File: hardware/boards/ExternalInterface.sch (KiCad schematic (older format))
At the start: 1 part, among them U1 ECP5UM5G-381caBGA

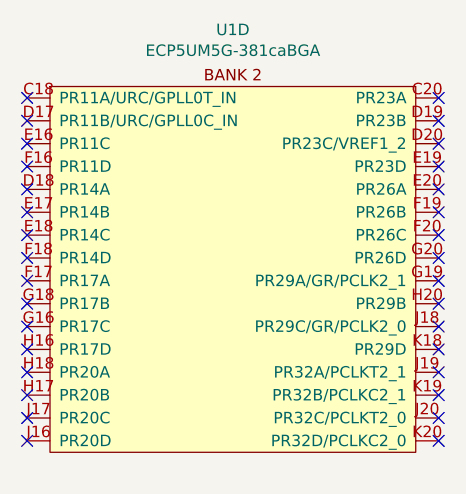
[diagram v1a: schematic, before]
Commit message: Moving banks around and rotated the FPGA to try and give the SERDES channels the best routing to the PCIe connector
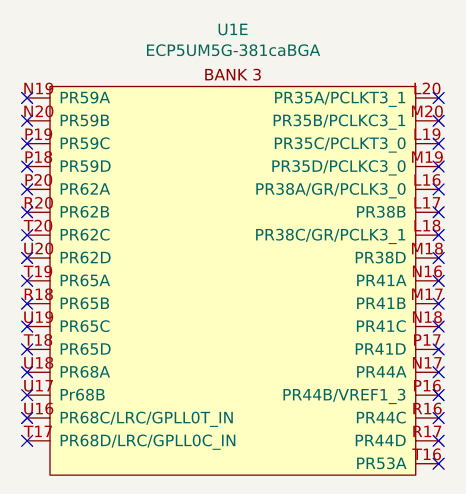
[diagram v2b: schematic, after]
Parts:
- removed U1: ECP5UM5G-381caBGA, lethalbit:318caBGA, symbol lethalbit:ECP5UM5G-381caBGA
- added U1: ECP5UM5G-381caBGA, lethalbit:318caBGA, symbol lethalbit:ECP5UM5G-381caBGA
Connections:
- no-connect marks 32 -> 33
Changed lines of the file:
@@
 Comment4 ""
 $EndDescr
-$Comp
-L lethalbit:ECP5UM5G-381caBGA U1
-U 4 1 5F2381FE
-P 5550 3250
-F 0 "U1" H 5550 3598 50  0000 C CNN
-F 1 "ECP5UM5G-381caBGA" H 5550 3507 50  0000 C CNN
-F 2 "lethalbit:318caBGA" H 4200 3400 50  0001 C CNN
-F 3 "" H 4200 3400 50  0001 C CNN
-F 4 "Lattice" H 5550 3250 50  0001 C CNN "MFR"
-F 5 "LFE5UM5G-85F-8BG381I" H 5550 3250 50  0001 C CNN "MPN"
-F 6 "220-2112-ND" H 5550 3250 50  0001 C CNN "DIGIKEY_PN"
-	4    5550 3250
-	1    0    0    -1
-$EndComp
 NoConn ~ 4650 3200
 NoConn ~ 4650 3300
@@
 NoConn ~ 6450 3300
 NoConn ~ 6450 3200
+$Comp
+L lethalbit:ECP5UM5G-381caBGA U?
+U 5 1 5F8BF516
+P 5550 3250
+AR Path="/5EF67D90/5F8BF516" Ref="U?"  Part="5"
+AR Path="/5F2CAFD2/5F8BF516" Ref="U?"  Part="5"
+AR Path="/5EF6A128/5F8BF516" Ref="U1"  Part="5"
+F 0 "U1" H 5550 3598 50  0000 C CNN
+F 1 "ECP5UM5G-381caBGA" H 5550 3507 50  0000 C CNN
+F 2 "lethalbit:318caBGA" H 4200 3400 50  0001 C CNN
+F 3 "" H 4200 3400 50  0001 C CNN
+F 4 "Lattice" H 5550 3250 50  0001 C CNN "MFR"
+F 5 "LFE5UM5G-85F-8BG381I" H 5550 3250 50  0001 C CNN "MPN"
+F 6 "220-2112-ND" H 5550 3250 50  0001 C CNN "DIGIKEY_PN"
+	5    5550 3250
+	-1   0    0    -1
+$EndComp
+NoConn ~ 6450 4800
 $EndSCHEMATC

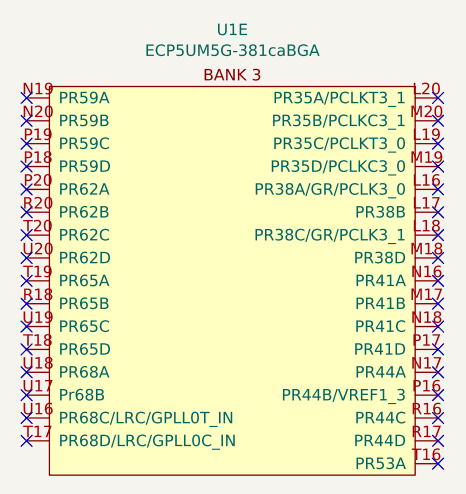
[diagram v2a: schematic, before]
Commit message: Moved some things around swapping the DDR from banks 7 and 8 to banks 2 and 3, and moved the GPIFF 2 stuff to bank 7 to stop them from crossing over
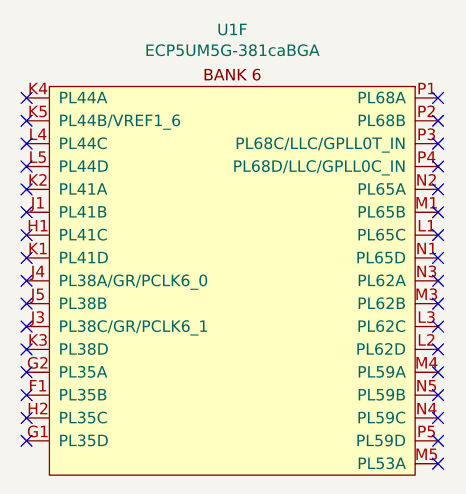
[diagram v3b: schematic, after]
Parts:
- removed U1: ECP5UM5G-381caBGA, lethalbit:318caBGA, symbol lethalbit:ECP5UM5G-381caBGA
- added U1: ECP5UM5G-381caBGA, lethalbit:318caBGA, symbol lethalbit:ECP5UM5G-381caBGA
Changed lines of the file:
@@
 NoConn ~ 6450 3300
 NoConn ~ 6450 3200
+NoConn ~ 6450 4800
 $Comp
 L lethalbit:ECP5UM5G-381caBGA U?
-U 5 1 5F8BF516
+U 6 1 5FCD2B63
 P 5550 3250
-AR Path="/5EF67D90/5F8BF516" Ref="U?"  Part="5"
-AR Path="/5F2CAFD2/5F8BF516" Ref="U?"  Part="5"
-AR Path="/5EF6A128/5F8BF516" Ref="U1"  Part="5"
+AR Path="/5EDF3898/5FCD2B63" Ref="U?"  Part="6"
+AR Path="/5FCD2B63" Ref="U?"  Part="6"
+AR Path="/5EF6A128/5FCD2B63" Ref="U1"  Part="6"
 F 0 "U1" H 5550 3598 50  0000 C CNN
 F 1 "ECP5UM5G-381caBGA" H 5550 3507 50  0000 C CNN
@@
 F 5 "LFE5UM5G-85F-8BG381I" H 5550 3250 50  0001 C CNN "MPN"
 F 6 "220-2112-ND" H 5550 3250 50  0001 C CNN "DIGIKEY_PN"
-	5    5550 3250
+	6    5550 3250
 	-1   0    0    -1
 $EndComp
-NoConn ~ 6450 4800
 $EndSCHEMATC

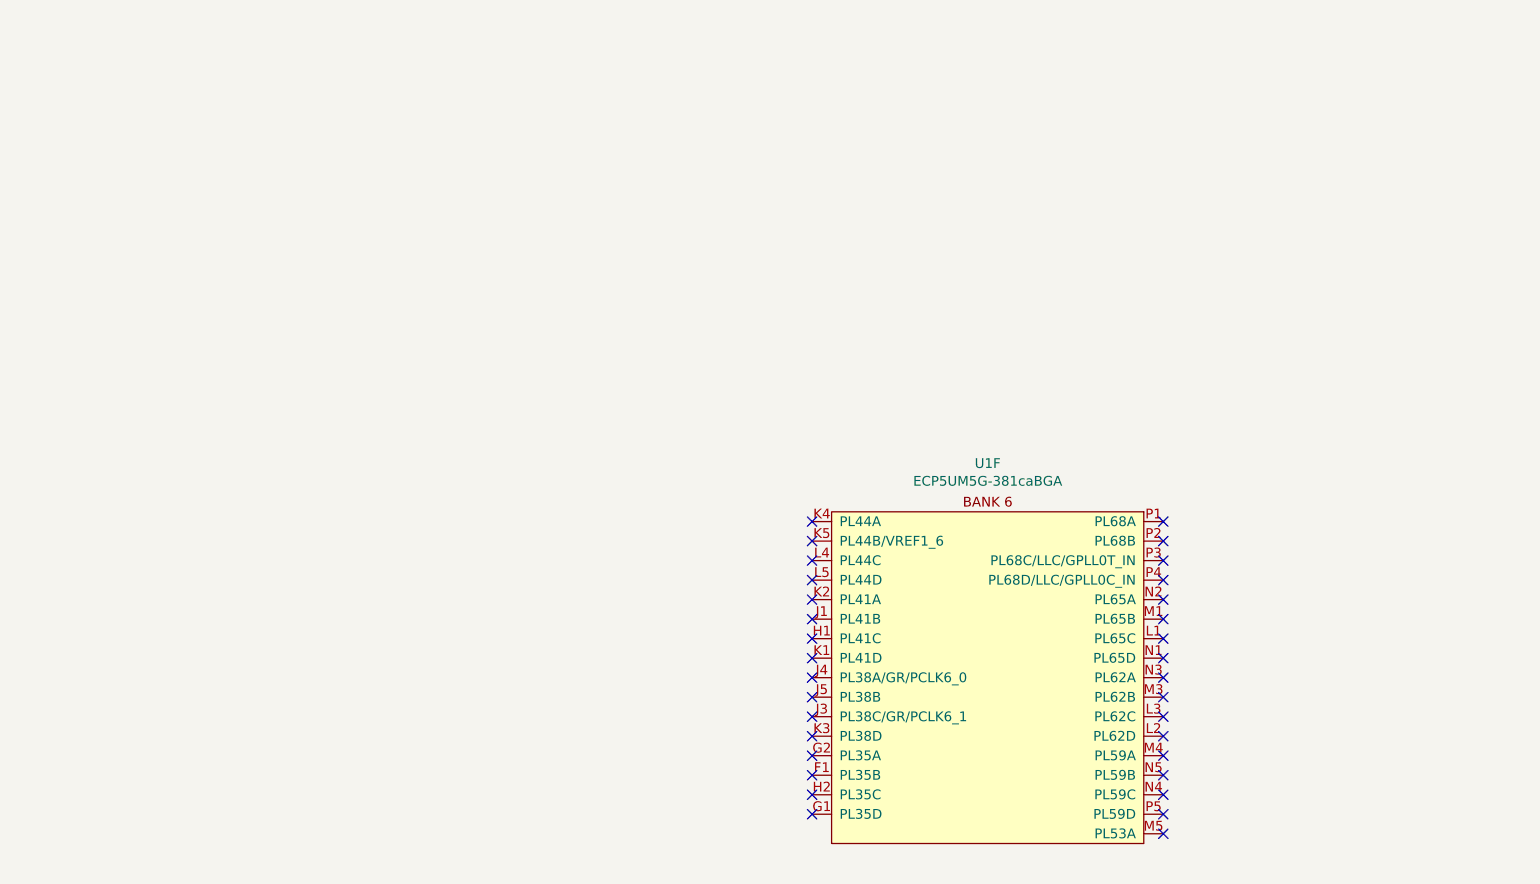
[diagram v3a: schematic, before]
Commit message: Moved some more banks around to try and keeps things from crossing over as much as possible
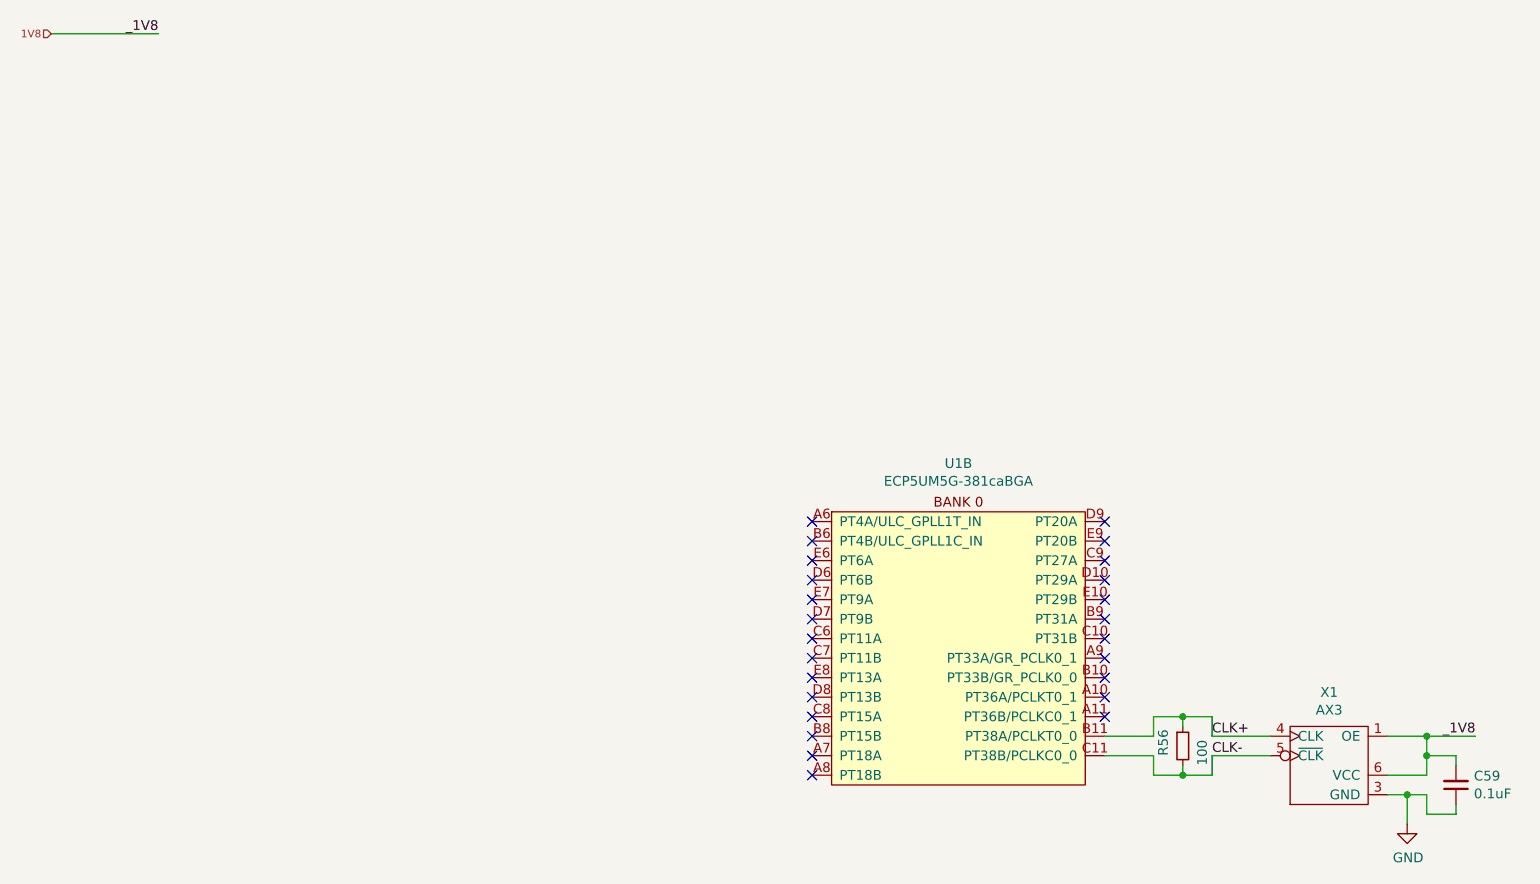
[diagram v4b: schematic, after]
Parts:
- removed U1: ECP5UM5G-381caBGA, lethalbit:318caBGA, symbol lethalbit:ECP5UM5G-381caBGA
- added C59: 0.1uF, Capacitor_SMD:C_0603_1608Metric, symbol Device:C_Small
- added R56: 100, Resistor_SMD:R_0402_1005Metric, symbol Device:R_Small
- added U1: ECP5UM5G-381caBGA, lethalbit:318caBGA, symbol lethalbit:ECP5UM5G-381caBGA
- added X1: AX3, lethalbit:AX3, symbol lethalbit:AX3
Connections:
- new net 1V8: C59.2, X1.1 (OE), X1.6 (VCC)
- new net CLK+: R56.1, U1.B11 (PT38A/PCLKT0_0), X1.4 (CLK)
- new net CLK-: R56.2, U1.C11 (PT38B/PCLKC0_0), X1.5 (~CLK)
- new net GND: C59.1, X1.3 (GND)
- no-connect marks 33 -> 25
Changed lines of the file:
@@
 NoConn ~ 4650 4400
 NoConn ~ 4650 4500
-NoConn ~ 4650 4600
-NoConn ~ 4650 4700
-NoConn ~ 6450 4700
-NoConn ~ 6450 4600
-NoConn ~ 6450 4500
-NoConn ~ 6450 4400
-NoConn ~ 6450 4300
-NoConn ~ 6450 4200
-NoConn ~ 6450 4100
-NoConn ~ 6450 4000
-NoConn ~ 6450 3900
-NoConn ~ 6450 3800
-NoConn ~ 6450 3700
-NoConn ~ 6450 3600
-NoConn ~ 6450 3500
-NoConn ~ 6450 3400
-NoConn ~ 6450 3300
-NoConn ~ 6450 3200
-NoConn ~ 6450 4800
+NoConn ~ 6150 4200
+NoConn ~ 6150 4100
+NoConn ~ 6150 4000
+NoConn ~ 6150 3900
+NoConn ~ 6150 3800
+NoConn ~ 6150 3700
+NoConn ~ 6150 3600
+NoConn ~ 6150 3500
+NoConn ~ 6150 3400
+NoConn ~ 6150 3300
+NoConn ~ 6150 3200
 $Comp
 L lethalbit:ECP5UM5G-381caBGA U?
-U 6 1 5FCD2B63
-P 5550 3250
-AR Path="/5EDF3898/5FCD2B63" Ref="U?"  Part="6"
-AR Path="/5FCD2B63" Ref="U?"  Part="6"
-AR Path="/5EF6A128/5FCD2B63" Ref="U1"  Part="6"
-F 0 "U1" H 5550 3598 50  0000 C CNN
-F 1 "ECP5UM5G-381caBGA" H 5550 3507 50  0000 C CNN
-F 2 "lethalbit:318caBGA" H 4200 3400 50  0001 C CNN
-F 3 "" H 4200 3400 50  0001 C CNN
-F 4 "Lattice" H 5550 3250 50  0001 C CNN "MFR"
-F 5 "LFE5UM5G-85F-8BG381I" H 5550 3250 50  0001 C CNN "MPN"
-F 6 "220-2112-ND" H 5550 3250 50  0001 C CNN "DIGIKEY_PN"
-	6    5550 3250
+U 2 1 5FD7F3DB
+P 5400 3250
+AR Path="/5EDAB834/5FD7F3DB" Ref="U?"  Part="2"
+AR Path="/5EF6A128/5FD7F3DB" Ref="U1"  Part="2"
+F 0 "U1" H 5400 3598 50  0000 C CNN
+F 1 "ECP5UM5G-381caBGA" H 5400 3507 50  0000 C CNN
+F 2 "lethalbit:318caBGA" H 4050 3400 50  0001 C CNN
+F 3 "" H 4050 3400 50  0001 C CNN
+F 4 "Lattice" H 5400 3250 50  0001 C CNN "MFR"
+F 5 "LFE5UM5G-85F-8BG381I" H 5400 3250 50  0001 C CNN "MPN"
+F 6 "220-2112-ND" H 5400 3250 50  0001 C CNN "DIGIKEY_PN"
+	2    5400 3250
+	1    0    0    -1
+$EndComp
+$Comp
+L lethalbit:AX3 X?
+U 1 1 5FDEF1C0
+P 7300 4450
+AR Path="/5EDAB834/5FDEF1C0" Ref="X?"  Part="1"
+AR Path="/5EF6A128/5FDEF1C0" Ref="X1"  Part="1"
+F 0 "X1" H 7300 4825 50  0000 C CNN
+F 1 "AX3" H 7300 4734 50  0000 C CNN
+F 2 "lethalbit:AX3" H 6950 4750 50  0001 C CNN
+F 3 "https://abracon.com/datasheets/AX3.pdf" H 6950 4750 50  0001 C CNN
+F 4 "Abracon LLC" H 7300 4450 50  0001 C CNN "MFR"
+F 5 "AX3DCF1-100.0000" H 7300 4450 50  0001 C CNN "MPN"
+	1    7300 4450
 	-1   0    0    -1
 $EndComp
+$Comp
+L Device:R_Small R?
+U 1 1 5FDEF1C8
+P 6550 4350
+AR Path="/5EDAB834/5FDEF1C8" Ref="R?"  Part="1"
+AR Path="/5EF6A128/5FDEF1C8" Ref="R56"  Part="1"
+F 0 "R56" V 6450 4300 50  0000 L CNN
+F 1 "100" V 6650 4250 50  0000 L CNN
+F 2 "Resistor_SMD:R_0402_1005Metric" H 6550 4350 50  0001 C CNN
+F 3 "~" H 6550 4350 50  0001 C CNN
+F 4 "Vishay Dale" H 6550 4350 50  0001 C CNN "MFR"
+F 5 "RCS0402100RFKED" V 6550 4350 50  0001 C CNN "MPN"
+	1    6550 4350
+	1    0    0    -1
+$EndComp
+Wire Wire Line
+	6150 4400 6400 4400
+Wire Wire Line
+	6400 4400 6400 4500
+Wire Wire Line
+	6400 4500 6550 4500
+Wire Wire Line
+	6700 4500 6700 4400
+Wire Wire Line
+	6700 4400 7000 4400
+Wire Wire Line
+	7000 4300 6700 4300
+Wire Wire Line
+	6700 4300 6700 4200
+Wire Wire Line
+	6700 4200 6550 4200
+Wire Wire Line
+	6400 4200 6400 4300
+Wire Wire Line
+	6400 4300 6150 4300
+Wire Wire Line
+	6550 4200 6550 4250
+Connection ~ 6550 4200
+Wire Wire Line
+	6550 4200 6400 4200
+Wire Wire Line
+	6550 4450 6550 4500
+Connection ~ 6550 4500
+Wire Wire Line
+	6550 4500 6700 4500
+$Comp
+L power:GND #PWR?
+U 1 1 5FDEF1DE
+P 7700 4750
+AR Path="/5EDAB834/5FDEF1DE" Ref="#PWR?"  Part="1"
+AR Path="/5EF6A128/5FDEF1DE" Ref="#PWR0139"  Part="1"
+F 0 "#PWR0139" H 7700 4500 50  0001 C CNN
+F 1 "GND" H 7705 4577 50  0000 C CNN
+F 2 "" H 7700 4750 50  0001 C CNN
+F 3 "" H 7700 4750 50  0001 C CNN
+	1    7700 4750
+	1    0    0    -1
+$EndComp
+Wire Wire Line
+	7600 4600 7700 4600
+Wire Wire Line
+	7700 4600 7700 4750
+$Comp
+L Device:C_Small C?
+U 1 1 5FDEF1E8
+P 7950 4550
+AR Path="/5EDF9F51/5FDEF1E8" Ref="C?"  Part="1"
+AR Path="/5EDAB834/5FDEF1E8" Ref="C?"  Part="1"
+AR Path="/5EF6A128/5FDEF1E8" Ref="C59"  Part="1"
+F 0 "C59" H 7858 4504 50  0000 R CNN
+F 1 "0.1uF" H 7858 4595 50  0000 R CNN
+F 2 "Capacitor_SMD:C_0603_1608Metric" H 7950 4550 50  0001 C CNN
+F 3 "~" H 7950 4550 50  0001 C CNN
+F 4 "KEMET" V 7950 4550 50  0001 C CNN "MFR"
+F 5 "C0603C104M5RACTU" V 7950 4550 50  0001 C CNN "MPN"
+	1    7950 4550
+	-1   0    0    1
+$EndComp
+Wire Wire Line
+	7700 4600 7800 4600
+Wire Wire Line
+	7800 4600 7800 4700
+Wire Wire Line
+	7800 4700 7950 4700
+Wire Wire Line
+	7950 4700 7950 4650
+Connection ~ 7700 4600
+Wire Wire Line
+	7600 4500 7800 4500
+Wire Wire Line
+	7800 4500 7800 4400
+Wire Wire Line
+	7800 4400 7950 4400
+Wire Wire Line
+	7950 4400 7950 4450
+Wire Wire Line
+	7600 4300 7800 4300
+Wire Wire Line
+	7800 4300 7800 4400
+Connection ~ 7800 4400
+Wire Wire Line
+	7800 4300 8050 4300
+Connection ~ 7800 4300
+Text Label 8050 4300 2    50   ~ 0
+_1V8
+Text Label 6700 4300 0    50   ~ 0
+CLK+
+Text Label 6700 4400 0    50   ~ 0
+CLK-
+Text HLabel 750  700  0    39   Input ~ 0
+1V8
+Wire Wire Line
+	750  700  1300 700
+Text Label 1300 700  2    50   ~ 0
+_1V8
 $EndSCHEMATC
